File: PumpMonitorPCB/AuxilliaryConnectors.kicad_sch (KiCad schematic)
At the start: 1 part

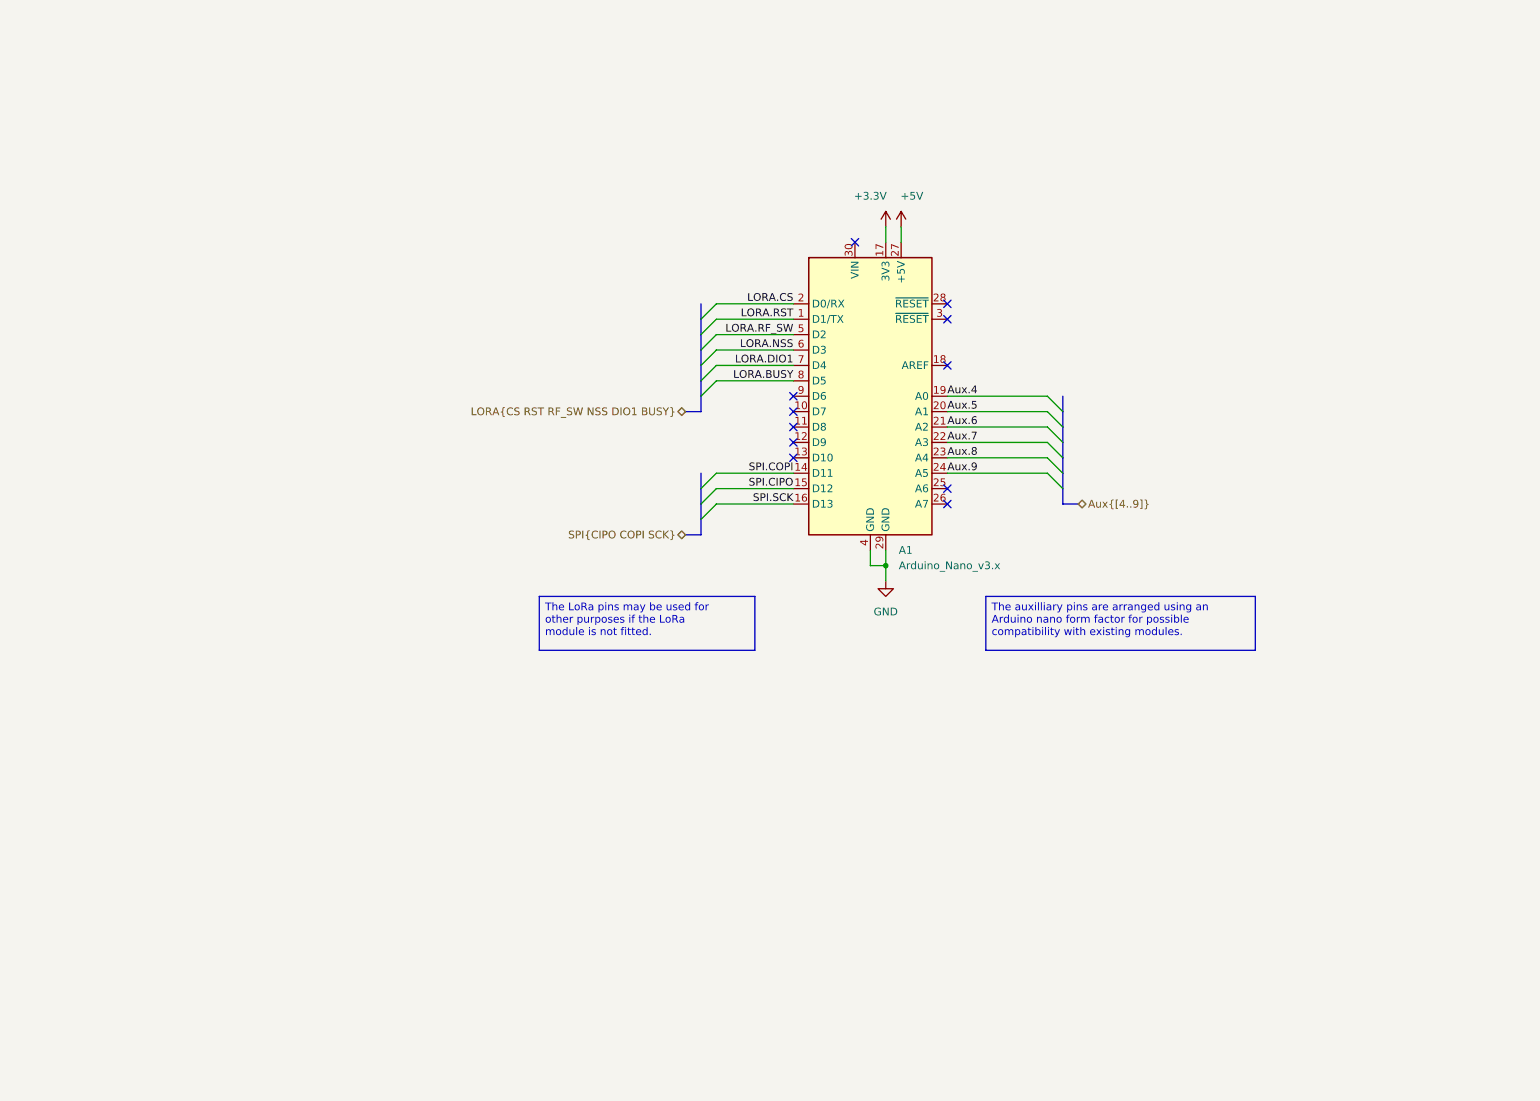
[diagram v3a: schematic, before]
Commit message: Rejigged auxilliary connectors, experimetning with kiclearance.
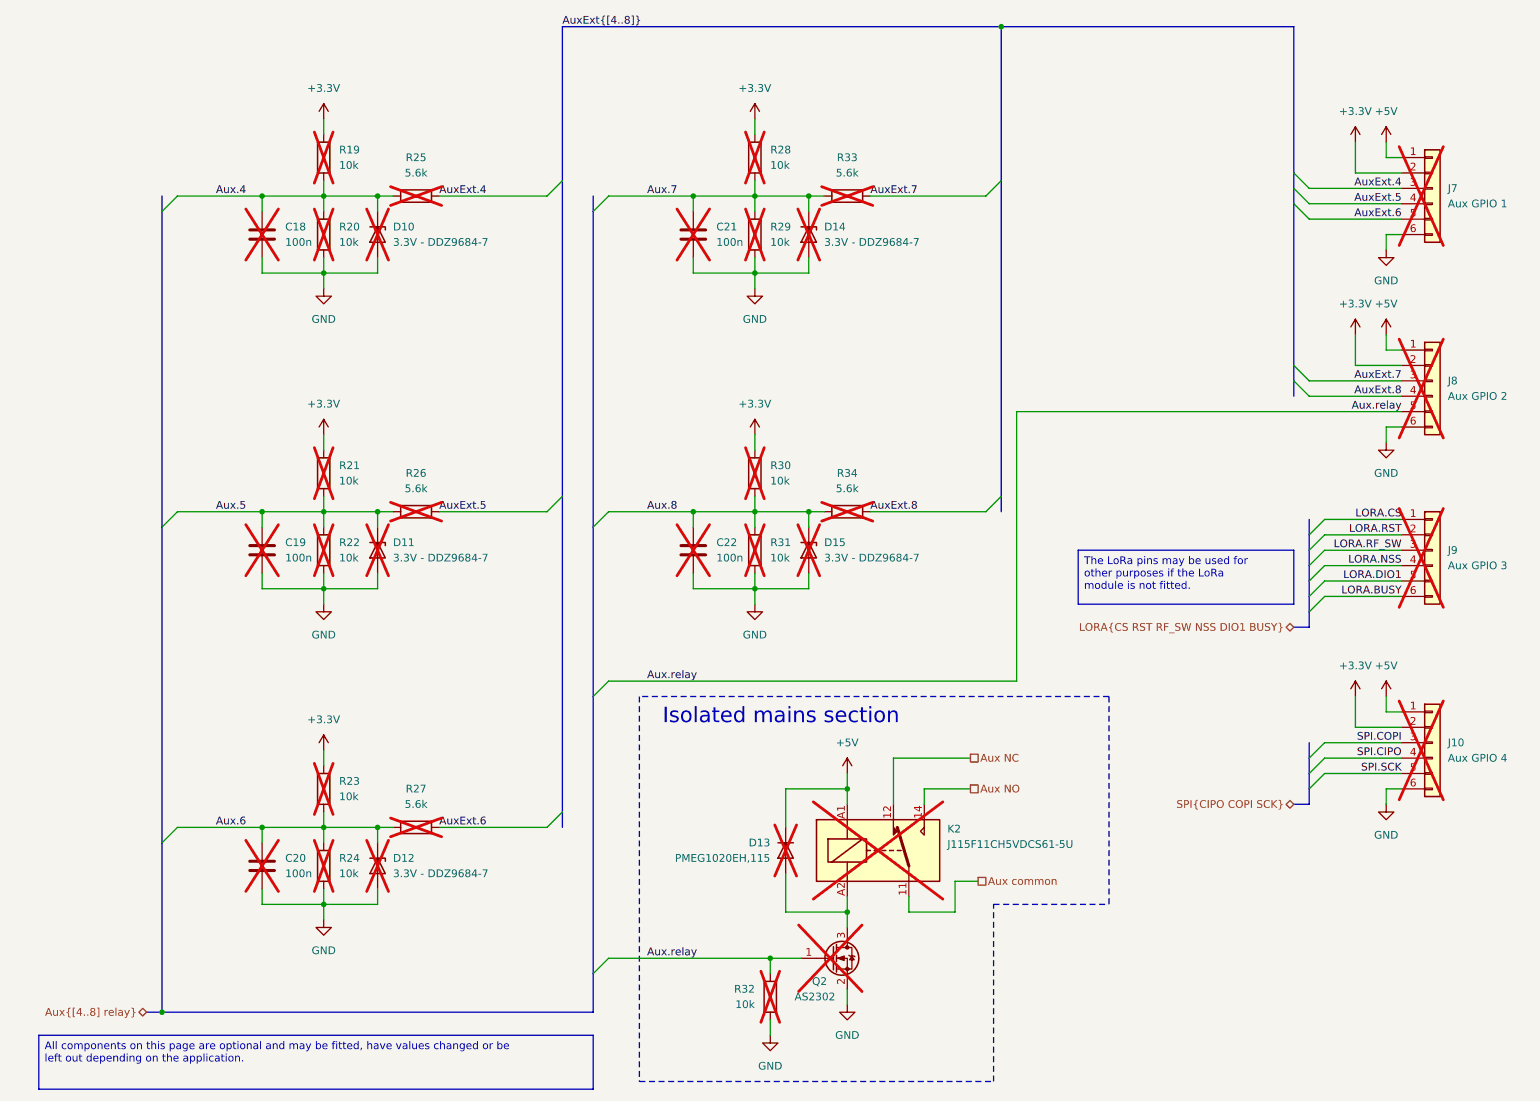
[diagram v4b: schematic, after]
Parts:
- removed A1: Arduino_Nano_v3.x, Module:Arduino_Nano, symbol MCU_Module:Arduino_Nano_v3.x
- added C18, C19, C20, C21, C22: 100n, Capacitor_SMD:C_0603_1608Metric_Pad1.08x0.95mm_HandSolder, symbol Device:C
- added D10, D11, D12, D14, D15: 3.3V - DDZ9684-7, Diode_SMD:D_SOD-123F, symbol Device:D_Zener
- added D13: PMEG1020EH,115, Diode_SMD:D_SOD-123F, symbol Diode:1N4004
- added J10: Aux GPIO 4, Connector_PinHeader_2.54mm:PinHeader_1x06_P2.54mm_Vertical, symbol Connector_Generic:Conn_01x06
- added J7: Aux GPIO 1, Connector_PinHeader_2.54mm:PinHeader_1x06_P2.54mm_Vertical, symbol Connector_Generic:Conn_01x06
- added J8: Aux GPIO 2, Connector_PinHeader_2.54mm:PinHeader_1x06_P2.54mm_Vertical, symbol Connector_Generic:Conn_01x06
- added J9: Aux GPIO 3, Connector_PinHeader_2.54mm:PinHeader_1x06_P2.54mm_Vertical, symbol Connector_Generic:Conn_01x06
- added K2: J115F11CH5VDCS61-5U, J115F11CH5VDCS61_5U_Relay:J115F11CH5VDCS61-5U, symbol Relay:Relay_SPDT
- added Q2: AS2302, Package_TO_SOT_SMD:TSOT-23, symbol Device:Q_NMOS_GSD
- added R19, R20, R21, R22, R23, R24, R28, R29, R30, R31, R32: 10k, Resistor_SMD:R_0603_1608Metric_Pad0.98x0.95mm_HandSolder, symbol Device:R
- added R25, R26, R27, R33, R34: 5.6k, Resistor_SMD:R_0603_1608Metric_Pad0.98x0.95mm_HandSolder, symbol Device:R
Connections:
- net +3.3V: now also J10.2 (Pin_2), J7.2 (Pin_2), J8.2 (Pin_2), R19.1, R21.1, R23.1, R28.1, R30.1
- net +5V: now also D13.1 (K), J10.1 (Pin_1), J7.1 (Pin_1), J8.1 (Pin_1), K2.A1
- net Aux.4: now also C18.1, D10.1 (K), R19.2, R20.1, R25.1
- net Aux.5: now also C19.1, D11.1 (K), R21.2, R22.1, R26.1
- net Aux.6: now also C20.1, D12.1 (K), R23.2, R24.1, R27.1
- net Aux.7: now also C21.1, D14.1 (K), R28.2, R29.1, R33.1
- net Aux.8: now also C22.1, D15.1 (K), R30.2, R31.1, R34.1
- net GND: now also C18.2, C19.2, C20.2, C21.2, C22.2, D10.2 (A), D11.2 (A), D12.2 (A), D14.2 (A), D15.2 (A), J10.6 (Pin_6), J7.6 (Pin_6), J8.6 (Pin_6), Q2.2 (S), R20.2, R22.2, R24.2, R29.2, R31.2, R32.2
- net LORA.BUSY: now also J9.6 (Pin_6)
- net LORA.CS: now also J9.1 (Pin_1)
- net LORA.DIO1: now also J9.5 (Pin_5)
- net LORA.NSS: now also J9.4 (Pin_4)
- net LORA.RF_SW: now also J9.3 (Pin_3)
- net LORA.RST: now also J9.2 (Pin_2)
- net SPI.CIPO: now also J10.4 (Pin_4)
- net SPI.COPI: now also J10.3 (Pin_3)
- net SPI.SCK: now also J10.5 (Pin_5)
- new net: D13.2 (A), K2.A2, Q2.3 (D)
- new net Aux NC: K2.12
- new net Aux NO: K2.14
- new net Aux common: K2.11
- new net Aux.relay: J8.5 (Pin_5), Q2.1 (G), R32.1
- new net AuxExt.4: J7.3 (Pin_3), R25.2
- new net AuxExt.5: J7.4 (Pin_4), R26.2
- new net AuxExt.6: J7.5 (Pin_5), R27.2
- new net AuxExt.7: J8.3 (Pin_3), R33.2
- new net AuxExt.8: J8.4 (Pin_4), R34.2
- no-connect marks 11 -> 0
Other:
- note added: "Isolated mains section"

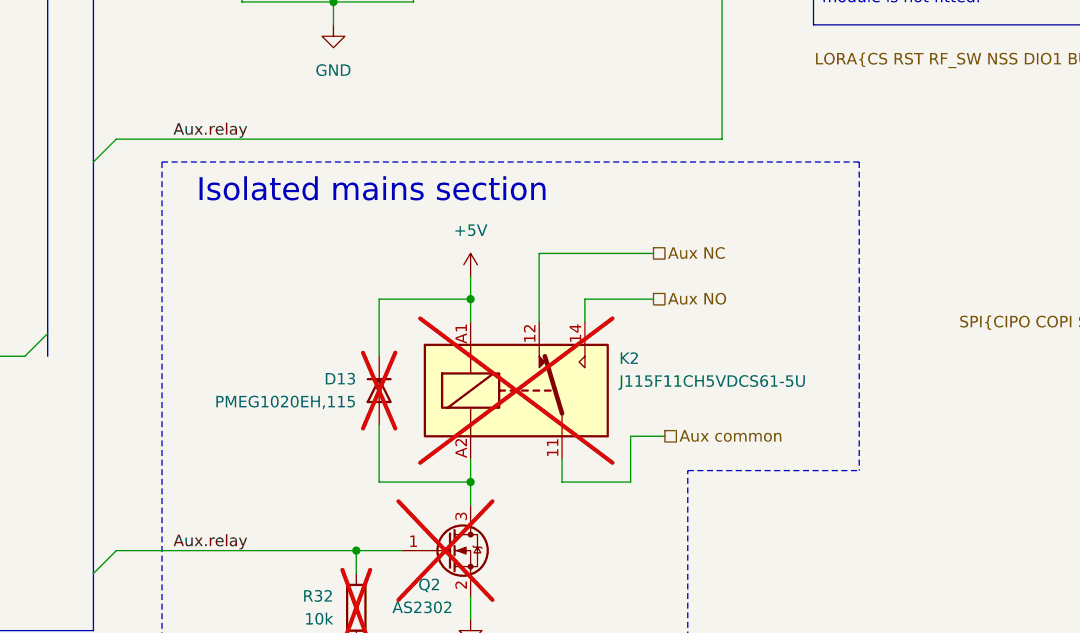
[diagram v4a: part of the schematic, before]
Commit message: Added fuse on aux relay, setting creepage and clearance distances.
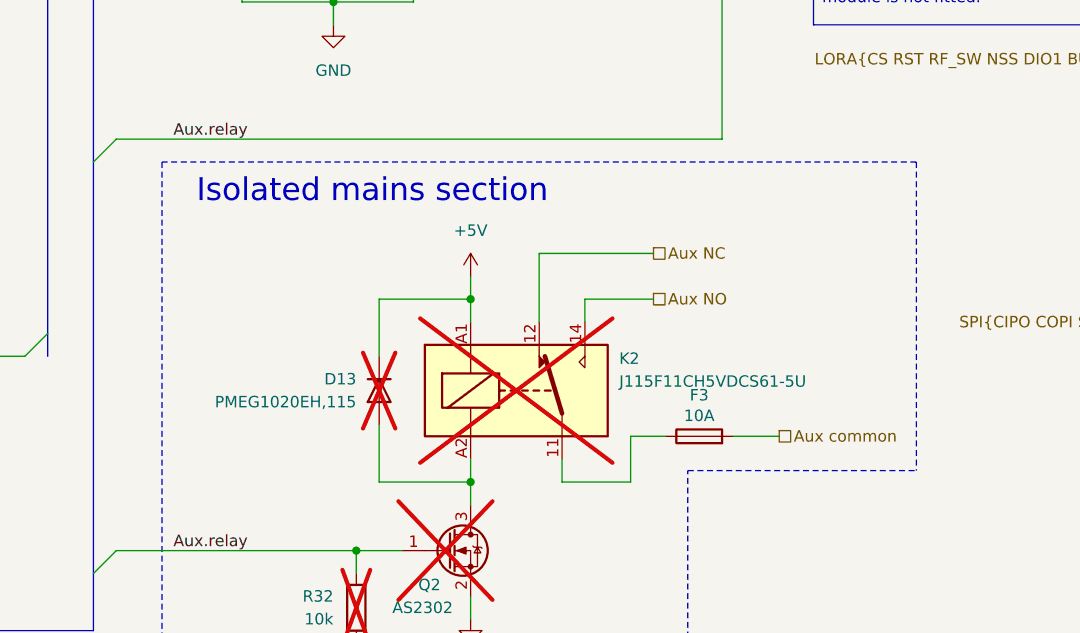
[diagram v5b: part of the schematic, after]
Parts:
- added F3: 10A, Fuse:Fuseholder_Cylinder-5x20mm_Stelvio-Kontek_PTF78_Horizontal_Open, symbol Device:Fuse
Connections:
- net Aux common: now also F3.2; no longer K2.11
- new net: F3.1, K2.11
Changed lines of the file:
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@@
 	(polyline
 		(pts
-			(xy 172.72 165.1) (xy 191.77 165.1)
+			(xy 172.72 165.1) (xy 198.12 165.1)
 		)
 		(stroke
@@
 	(wire
 		(pts
+			(xy 177.8 161.29) (xy 182.88 161.29)
+		)
+		(stroke
+			(width 0)
+			(type default)
+		)
+	)
+	(wire
+		(pts
 			(xy 142.24 110.49) (xy 142.24 113.03)
 		)
@@
 	(polyline
 		(pts
-			(xy 191.77 130.81) (xy 191.77 165.1)
+			(xy 198.12 130.81) (xy 198.12 165.1)
 		)
 		(stroke
@@
 	(polyline
 		(pts
-			(xy 191.77 130.81) (xy 114.3 130.81)
+			(xy 198.12 130.81) (xy 114.3 130.81)
 		)
 		(stroke
@@
 	(hierarchical_label "Aux common"
 		(shape passive)
-		(at 170.18 161.29 0)
+		(at 182.88 161.29 0)
 		(effects
 			(font
@@
 		(length 2.54)
 		(shape round)
+		(at 180.34 161.29 0)
+		(fields_autoplaced yes)
+		(effects
+			(font
+				(size 1.27 1.27)
+			)
+			(justify left bottom)
+		)
+		(property "Netclass" "HV"
+			(at 181.0385 158.75 0)
+			(effects
+				(font
+					(size 1.27 1.27)
+				)
+				(justify left)
+			)
+		)
+		(property "Component Class" ""
+			(at 55.88 123.19 0)
+			(effects
+				(font
+					(size 1.27 1.27)
+					(italic yes)
+				)
+			)
+		)
+	)
+	(netclass_flag ""
+		(length 2.54)
+		(shape round)
 		(at 114.3 78.74 0)
 		(fields_autoplaced yes)
@@
 					(unit 1)
 				)
+			)
+		)
+	)
+	(symbol
+		(lib_id "Device:Fuse")
+		(at 173.99 161.29 90)
+		(unit 1)
+		(exclude_from_sim no)
+		(in_bom yes)
+		(on_board yes)
+		(dnp no)
+		(property "Reference" "F3"
+			(at 173.99 156.718 90)
+			(effects
+				(font
+					(size 1.27 1.27)
+				)
+			)
+		)
+		(property "Value" "10A"
+			(at 173.99 159.004 90)
+			(effects
+				(font
+					(size 1.27 1.27)
+				)
+			)
+		)
+		(property "Footprint" "Fuse:Fuseholder_Cylinder-5x20mm_Stelvio-Kontek_PTF78_Horizontal_Open"
+			(at 173.99 163.068 90)
+			(effects
+				(font
+					(size 1.27 1.27)
+				)
+				(hide yes)
+			)
+		)
+		(property "Datasheet" "~"
+			(at 173.99 161.29 0)
+			(effects
+				(font
+					(size 1.27 1.27)
+				)
+				(hide yes)
+			)
+		)
+		(property "Description" "Fuse"
+			(at 173.99 161.29 0)
+			(effects
+				(font
+					(size 1.27 1.27)
+				)
+				(hide yes)
+			)
+		)
+		(property "Part number" "696103201002"
+			(at 173.99 161.29 90)
+			(effects
+				(font
+					(size 1.27 1.27)
+				)
+				(hide yes)
+			)
+		)
+		(pin "2"
+		)
+		(pin "1"
+		)
+		(instances
+			(project "PumpMonitorPCB"
+				(path "/c90c4964-ca1b-44d9-8ea9-8989903af0f2/519408a1-89cc-4bd2-9b7b-cb03d2ff4d33/91bf94f0-7f00-44b4-9278-0ffa2bbc6ab6"
+					(reference "F3")
+					(unit 1)
+				)

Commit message: Adding test points, CAD files
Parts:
- C18, C19, C20, C21, C22: DigikeyNumber (none) -> 311-1088-1-ND
- D10, D11, D12, D14, D15: DigikeyNumber (none) -> DDZ9684-7DICT-ND
- D13: DigikeyNumber (none) -> 1727-3849-1-ND
- F3: DigikeyNumber (none) -> 732-11372-ND
- K2: DigikeyNumber (none) -> 2449-J115F11CH5VDCS61.5U-ND
- Q2: DigikeyNumber (none) -> 4530-AS2302CT-ND
